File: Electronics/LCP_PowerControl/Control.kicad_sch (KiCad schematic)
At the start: 3 parts, among them J2 Conn_01x05, J4 Conn_01x05

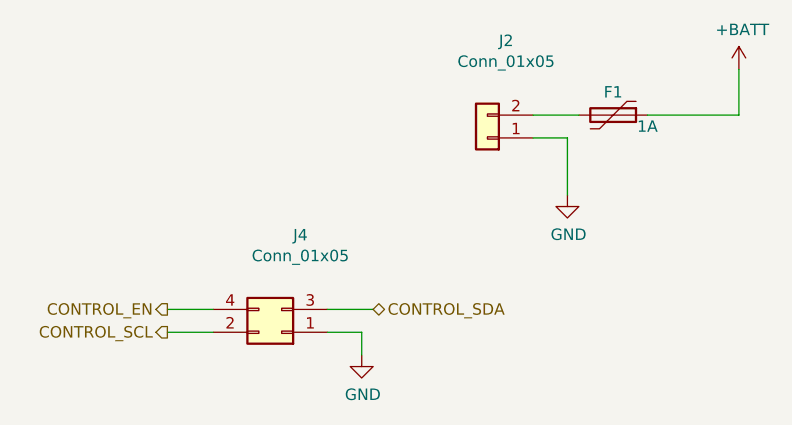
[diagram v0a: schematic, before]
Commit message: Updated Connectors
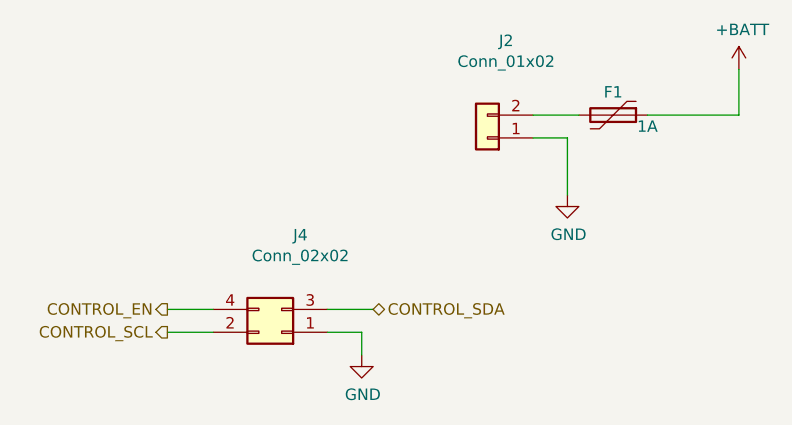
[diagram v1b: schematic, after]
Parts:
- J2: value Conn_01x05 -> Conn_01x02; MPN 61300511121 -> 0430450212
- J4: value Conn_01x05 -> Conn_02x02; MPN 61300511121 -> 0430450428
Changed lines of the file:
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@@
   (paper "A4")
   (title_block
-    (date "2020-06-17")
-    (rev "R0.1")
+    (date "2024-07-22")
+    (rev "1.3")
     (comment 1 "Design by: Matt Casari")
+    (comment 2 "Updated by Joseph Kurina")
   )
   (wire (pts (xy 97.79 115.57) (xy 93.98 115.57))
@@
       (effects (font (size 1.27 1.27)))
     )
-    (property "Value" "Conn_01x05" (at 113.8428 85.4964 0)
+    (property "Value" "Conn_01x02" (at 113.8428 85.4964 0)
       (effects (font (size 1.27 1.27)))
     )
@@
       (effects (font (size 1.27 1.27)) hide)
     )
-    (property "MPN" "61300511121" (at 111.76 93.98 0)
+    (property "MPN" "0430450212" (at 111.76 93.98 0)
       (effects (font (size 1.27 1.27)) hide)
     )
@@
       (effects (font (size 1.27 1.27)))
     )
-    (property "Value" "Conn_01x05" (at 90.9828 107.0864 0)
+    (property "Value" "Conn_02x02" (at 90.9828 107.0864 0)
       (effects (font (size 1.27 1.27)))
     )
@@
       (effects (font (size 1.27 1.27)) hide)
     )
-    (property "MPN" "61300511121" (at 88.9 115.57 0)
+    (property "MPN" "0430450428" (at 88.9 115.57 0)
       (effects (font (size 1.27 1.27)) hide)
     )
